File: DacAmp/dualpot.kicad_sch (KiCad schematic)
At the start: 0 parts

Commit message: add basic amp architecture
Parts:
- added RV2: R_Potentiometer_Dual, symbol Device:R_Potentiometer_Dual
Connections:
- new net FILT_OUT_L: RV2.4
- new net FILT_OUT_R: RV2.1
- new net POT_WIPER_L: RV2.5
- new net POT_WIPER_R: RV2.2
- new net VOL_CTRL_OUT_R: RV2.3, RV2.6
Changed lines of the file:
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@@
 	(generator "eeschema")
 	(generator_version "8.0")
-	(paper "A4")
+	(paper "A5")
+	(wire
+		(pts
+			(xy 92.71 55.88) (xy 97.79 55.88)
+		)
+		(stroke
+			(width 0)
+			(type default)
+		)
+	)
+	(wire
+		(pts
+			(xy 120.65 55.88) (xy 118.11 55.88)
+		)
+		(stroke
+			(width 0)
+			(type default)
+		)
+	)
+	(wire
+		(pts
+			(xy 109.22 55.88) (xy 110.49 55.88)
+		)
+		(stroke
+			(width 0)
+			(type default)
+		)
+	)
+	(wire
+		(pts
+			(xy 120.65 64.77) (xy 120.65 55.88)
+		)
+		(stroke
+			(width 0)
+			(type default)
+		)
+	)
+	(wire
+		(pts
+			(xy 105.41 55.88) (xy 105.41 64.77)
+		)
+		(stroke
+			(width 0)
+			(type default)
+		)
+	)
+	(wire
+		(pts
+			(xy 109.22 64.77) (xy 109.22 55.88)
+		)
+		(stroke
+			(width 0)
+			(type default)
+		)
+	)
+	(hierarchical_label "POT_WIPER_R"
+		(shape output)
+		(at 101.6 50.8 90)
+		(fields_autoplaced yes)
+		(effects
+			(font
+				(size 1.27 1.27)
+			)
+			(justify left)
+		)
+	)
+	(hierarchical_label "POT_WIPER_L"
+		(shape output)
+		(at 114.3 50.8 90)
+		(fields_autoplaced yes)
+		(effects
+			(font
+				(size 1.27 1.27)
+			)
+			(justify left)
+		)
+	)
+	(hierarchical_label "FILT_OUT_L"
+		(shape input)
+		(at 109.22 64.77 270)
+		(fields_autoplaced yes)
+		(effects
+			(font
+				(size 1.27 1.27)
+			)
+			(justify right)
+		)
+	)
+	(hierarchical_label "VOL_CTRL_OUT_R"
+		(shape output)
+		(at 120.65 64.77 270)
+		(fields_autoplaced yes)
+		(effects
+			(font
+				(size 1.27 1.27)
+			)
+			(justify right)
+		)
+	)
+	(hierarchical_label "FILT_OUT_R"
+		(shape input)
+		(at 92.71 55.88 180)
+		(fields_autoplaced yes)
+		(effects
+			(font
+				(size 1.27 1.27)
+			)
+			(justify right)
+		)
+	)
+	(hierarchical_label "VOL_CTRL_OUT_R"
+		(shape output)
+		(at 105.41 64.77 270)
+		(fields_autoplaced yes)
+		(effects
+			(font
+				(size 1.27 1.27)
+			)
+			(justify right)
+		)
+	)
+	(symbol
+		(lib_id "Device:R_Potentiometer_Dual")
+		(at 107.95 53.34 0)
+		(unit 1)
+		(exclude_from_sim no)
+		(in_bom yes)
+		(on_board yes)
+		(dnp no)
+		(fields_autoplaced yes)
+		(property "Reference" "RV2"
+			(at 107.95 59.69 0)
+			(effects
+				(font
+					(size 1.27 1.27)
+				)
+			)
+		)
+		(property "Value" "R_Potentiometer_Dual"
+			(at 107.95 62.23 0)
+			(effects
+				(font
+					(size 1.27 1.27)
+				)
+			)
+		)
+		(property "Footprint" ""
+			(at 114.3 55.245 0)
+			(effects
+				(font
+					(size 1.27 1.27)
+				)
+				(hide yes)
+			)
+		)
+		(property "Datasheet" "~"
+			(at 114.3 55.245 0)
+			(effects
+				(font
+					(size 1.27 1.27)
+				)
+				(hide yes)
+			)
+		)
+		(property "Description" "Dual potentiometer"
+			(at 107.95 53.34 0)
+			(effects
+				(font
+					(size 1.27 1.27)
+				)
+				(hide yes)
+			)
+		)
+		(pin "5"
+		)
+		(pin "3"
+		)
+		(pin "4"
+		)
+		(pin "2"
+		)
+		(pin "1"
+		)
+		(pin "6"
+		)
+		(instances)
+	)
 )

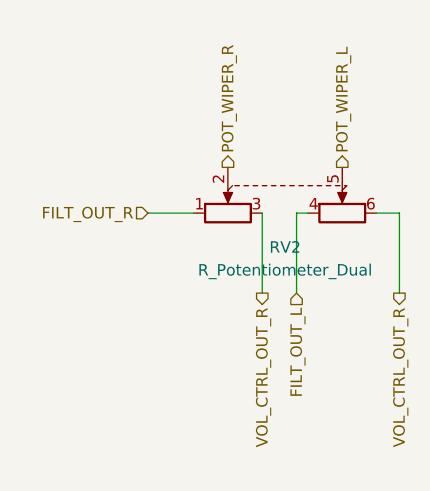
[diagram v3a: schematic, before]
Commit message: complete overall schematic, TODO: find values and add net labels
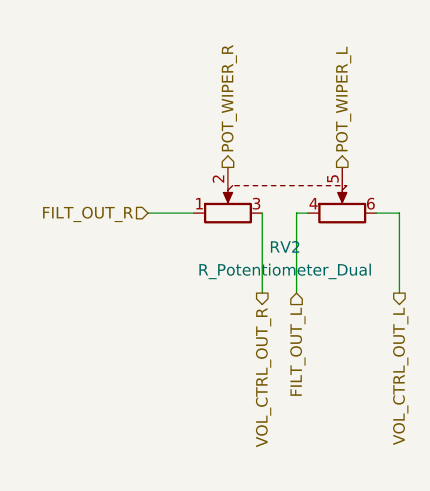
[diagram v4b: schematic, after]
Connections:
- net VOL_CTRL_OUT_R: no longer RV2.6
- new net VOL_CTRL_OUT_L: RV2.6
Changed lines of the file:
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@@
 		)
 	)
-	(hierarchical_label "VOL_CTRL_OUT_R"
+	(hierarchical_label "VOL_CTRL_OUT_L"
 		(shape output)
 		(at 120.65 64.77 270)

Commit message: add components and footprints
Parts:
- RV2: footprint (none) -> potentiometer:POT_PTN16-A10220K1B2
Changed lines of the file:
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@@
 			)
 		)
-		(property "Footprint" ""
+		(property "Footprint" "potentiometer:POT_PTN16-A10220K1B2"
 			(at 114.3 55.245 0)
 			(effects
